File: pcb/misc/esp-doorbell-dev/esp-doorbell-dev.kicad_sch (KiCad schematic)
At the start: 26 parts, among them J1 JST XH, J2 Screw_Terminal_01x02, J3 JST XH/PH, J4 JST PH, Q1 BSS84, Q2 BSS84, Q3 BSS84, Q4 2N7002DW, Q5 BSS138, U1 WS2811F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

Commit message: Migrate `WS2811F` symbol from `lcsc` to `ic`
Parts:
- U1: symbol lcsc:WS2811F -> ic:WS2811F
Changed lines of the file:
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@@
 	)
 	(symbol
-		(lib_id "lcsc:WS2811F")
+		(lib_id "ic:WS2811F")
 		(at 105.41 44.45 0)
 		(unit 1)

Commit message: Migrate `LD2410C` symbol from `lcsc` to `modules`
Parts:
- SM4: symbol lcsc:HLK-LD2410C-P -> modules:LD2410C
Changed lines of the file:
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@@
 	)
 	(symbol
-		(lib_id "lcsc:HLK-LD2410C-P")
+		(lib_id "modules:LD2410C")
 		(at 255.27 41.91 0)
 		(unit 1)

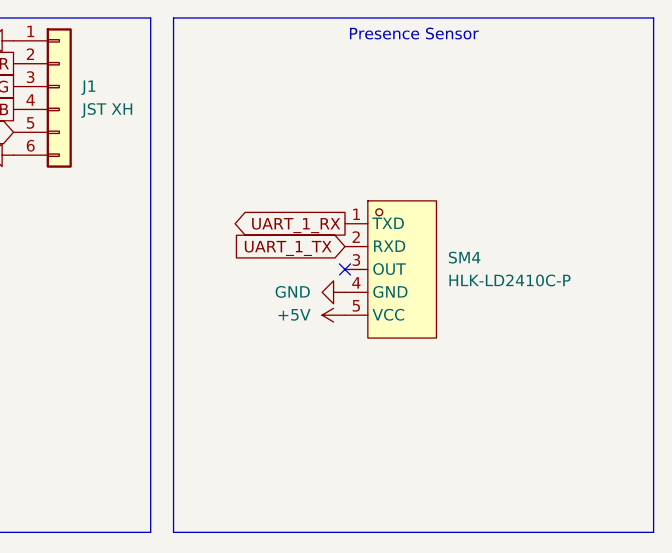
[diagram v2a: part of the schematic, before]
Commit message: Rework `HLK-LD2410C` to match KiCAD symbol conventions
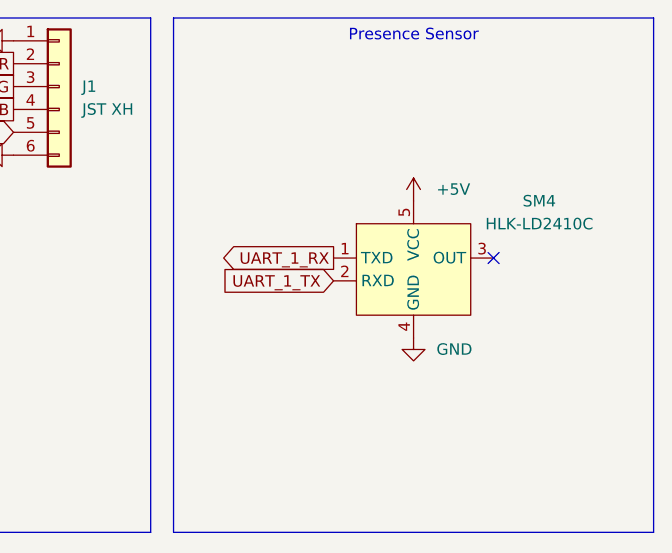
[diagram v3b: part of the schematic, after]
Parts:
- removed SM4: HLK-LD2410C-P, lcsc:SENSOR-TH_HLK-LD2410C-P, symbol modules:LD2410C
- added SM4: HLK-LD2410C, lcsc:SENSOR-TH_HLK-LD2410C-P, symbol module:HLK-LD2410C
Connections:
- net +5V: now also SM4.5 (VCC)
- net GND: now also SM4.4 (GND)
- net UART_1_RX: now also SM4.1 (TXD)
- net UART_1_TX: now also SM4.2 (RXD)
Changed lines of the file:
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@@
 	)
 	(no_connect
-		(at 248.92 41.91)
+		(at 265.43 40.64)
 	)
 	(no_connect
@@
 	(global_label "UART_1_TX"
 		(shape input)
-		(at 248.92 39.37 180)
+		(at 247.65 43.18 180)
 		(fields_autoplaced yes)
 		(effects
@@
 		)
 		(property "Intersheetrefs" "${INTERSHEET_REFS}"
-			(at 235.9563 39.37 0)
+			(at 234.6863 43.18 0)
 			(effects
 				(font
@@
 	(global_label "UART_1_RX"
 		(shape output)
-		(at 248.92 36.83 180)
+		(at 247.65 40.64 180)
 		(fields_autoplaced yes)
 		(effects
@@
 		)
 		(property "Intersheetrefs" "${INTERSHEET_REFS}"
-			(at 235.6539 36.83 0)
+			(at 234.3839 40.64 0)
 			(effects
 				(font
@@
 	(symbol
 		(lib_id "power:GND")
-		(at 248.92 44.45 270)
+		(at 256.54 49.53 0)
 		(unit 1)
 		(exclude_from_sim no)
@@
 		(fields_autoplaced yes)
 		(property "Reference" "#PWR010"
-			(at 242.57 44.45 0)
+			(at 256.54 55.88 0)
 			(effects
 				(font
@@
 		)
 		(property "Value" "GND"
-			(at 245.11 44.4499 90)
+			(at 259.08 50.7999 0)
 			(effects
 				(font
 					(size 1.27 1.27)
 				)
-				(justify right)
+				(justify left)
 			)
 		)
 		(property "Footprint" ""
-			(at 248.92 44.45 0)
+			(at 256.54 49.53 0)
 			(effects
 				(font
@@
 		)
 		(property "Datasheet" ""
-			(at 248.92 44.45 0)
+			(at 256.54 49.53 0)
 			(effects
 				(font
@@
 		)
 		(property "Description" "Power symbol creates a global label with name \"GND\" , ground"
-			(at 248.92 44.45 0)
+			(at 256.54 49.53 0)
 			(effects
 				(font
@@
 	)
 	(symbol
-		(lib_id "modules:LD2410C")
-		(at 255.27 41.91 0)
-		(unit 1)
-		(exclude_from_sim no)
-		(in_bom yes)
-		(on_board yes)
-		(dnp no)
-		(fields_autoplaced yes)
-		(property "Reference" "SM4"
-			(at 260.35 40.6399 0)
-			(effects
-				(font
-					(size 1.27 1.27)
-				)
-				(justify left)
-			)
-		)
-		(property "Value" "HLK-LD2410C-P"
-			(at 260.35 43.1799 0)
-			(effects
-				(font
-					(size 1.27 1.27)
-				)
-				(justify left)
-			)
-		)
-		(property "Footprint" "lcsc:SENSOR-TH_HLK-LD2410C-P"
-			(at 255.27 54.61 0)
-			(effects
-				(font
-					(size 1.27 1.27)
-				)
-				(hide yes)
-			)
-		)
-		(property "Datasheet" ""
-			(at 255.27 41.91 0)
-			(effects
-				(font
-					(size 1.27 1.27)
-				)
-				(hide yes)
-			)
-		)
-		(property "Description" ""
-			(at 255.27 41.91 0)
-			(effects
-				(font
-					(size 1.27 1.27)
-				)
-				(hide yes)
-			)
-		)
-		(property "LCSC Part" "C19723500"
-			(at 255.27 57.15 0)
-			(effects
-				(font
-					(size 1.27 1.27)
-				)
-				(hide yes)
-			)
-		)
-		(pin "1"
-		)
-		(pin "3"
-		)
-		(pin "2"
-		)
-		(pin "4"
-		)
-		(pin "5"
-		)
-		(instances
-			(project ""
-				(path "/76a56607-25e2-40a3-9282-ff279b153f75"
-					(reference "SM4")
-					(unit 1)
-				)
-			)
-		)
-	)
-	(symbol
 		(lib_id "power:+5V")
 		(at 137.16 86.36 90)
@@
 	(symbol
 		(lib_id "power:+5V")
-		(at 248.92 46.99 90)
+		(at 256.54 34.29 0)
 		(unit 1)
 		(exclude_from_sim no)
@@
 		(fields_autoplaced yes)
 		(property "Reference" "#PWR09"
-			(at 252.73 46.99 0)
+			(at 256.54 38.1 0)
 			(effects
 				(font
@@
 		)
 		(property "Value" "+5V"
-			(at 245.11 46.9899 90)
+			(at 259.08 33.0199 0)
 			(effects
 				(font
@@
 		)
 		(property "Footprint" ""
-			(at 248.92 46.99 0)
+			(at 256.54 34.29 0)
 			(effects
 				(font
@@
 		)
 		(property "Datasheet" ""
-			(at 248.92 46.99 0)
+			(at 256.54 34.29 0)
 			(effects
 				(font
@@
 		)
 		(property "Description" "Power symbol creates a global label with name \"+5V\""
-			(at 248.92 46.99 0)
+			(at 256.54 34.29 0)
 			(effects
 				(font
@@
 					(unit 1)
 				)
+			)
+		)
+	)
+	(symbol
+		(lib_id "module:HLK-LD2410C")
+		(at 256.54 41.91 0)
+		(unit 1)
+		(exclude_from_sim no)
+		(in_bom yes)
+		(on_board yes)
+		(dnp no)
+		(fields_autoplaced yes)
+		(property "Reference" "SM4"
+			(at 270.51 34.3214 0)
+			(effects
+				(font
+					(size 1.27 1.27)
+				)
+			)
+		)
+		(property "Value" "HLK-LD2410C"
+			(at 270.51 36.8614 0)
+			(effects
+				(font
+					(size 1.27 1.27)
+				)
+			)
+		)
+		(property "Footprint" "lcsc:SENSOR-TH_HLK-LD2410C-P"
+			(at 256.54 54.61 0)
+			(effects
+				(font
+					(size 1.27 1.27)
+				)
+				(hide yes)
+			)
+		)
+		(property "Datasheet" "https://www.lcsc.com/datasheet/lcsc_datasheet_2409141622_HI-LINK-HLK-LD2410C-P_C19723500.pdf"
+			(at 275.59 46.99 0)
+			(effects
+				(font
+					(size 1.27 1.27)
+				)
+				(hide yes)
+			)
+		)
+		(property "Description" "Human Presence Sensor, Millimeter Wave Radar, Bluetooth Low Energy/UART module"
+			(at 275.59 46.99 0)
+			(effects
+				(font
+					(size 1.27 1.27)
+				)
+				(hide yes)
+			)
+		)
+		(property "LCSC Part" "C19723500"
+			(at 256.54 57.15 0)
+			(effects
+				(font
+					(size 1.27 1.27)
+				)
+				(hide yes)
+			)
+		)
+		(pin "3"
+		)
+		(pin "5"
+		)
+		(pin "4"
+		)
+		(pin "2"
+		)
+		(pin "1"
+		)
+		(instances
+			(project ""
+				(path "/76a56607-25e2-40a3-9282-ff279b153f75"
+					(reference "SM4")
+					(unit 1)
+				)

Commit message: Migrate HLK-LD2410C module footprint from `lcsc` to `module`
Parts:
- SM4: footprint lcsc:SENSOR-TH_HLK-LD2410C-P -> module:HLK-LD2410C-module
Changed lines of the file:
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@@
 			)
 		)
-		(property "Footprint" "lcsc:SENSOR-TH_HLK-LD2410C-P"
+		(property "Footprint" "module:HLK-LD2410C-module"
 			(at 256.54 54.61 0)
 			(effects

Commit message: Migrate G3MB-202P footprint from `custom` to `discrete`
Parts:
- U2: footprint custom:RELAY-G3MB-202P-5VDC -> discrete:Relay_G3MB-202P
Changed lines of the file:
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@@
 			)
 		)
-		(property "Footprint" "custom:RELAY-G3MB-202P-5VDC"
+		(property "Footprint" "discrete:Relay_G3MB-202P"
 			(at 167.64 123.19 0)
 			(effects

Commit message: Migrate 3.5mm 1x02 terminal block footprint to `connector`
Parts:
- J2: footprint custom:TerminalBlock_Phoenix_PT-1,5-2-3.5-H_1x02_P3.50mm_Horizontal_custom -> connector:TerminalBlock_Phoenix_PT-1,5-2-3.5-H_1x02_P3.50mm_Horizontal
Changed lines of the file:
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@@
 			)
 		)
-		(property "Footprint" "custom:TerminalBlock_Phoenix_PT-1,5-2-3.5-H_1x02_P3.50mm_Horizontal_custom"
+		(property "Footprint" "connector:TerminalBlock_Phoenix_PT-1,5-2-3.5-H_1x02_P3.50mm_Horizontal"
 			(at 175.26 86.36 0)
 			(effects

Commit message: Reduce custom footprint use on esp-doorbell-dev
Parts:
- Q4: footprint package:SOT-363_SC-70-6 -> package:SOT-363_SC-70-6_HandSolder
- Q5: footprint package:SOT-23 -> Package_TO_SOT_SMD:SOT-23
- R3, R4, R5: footprint custom:R_0603_1608Metric_Pad0.98x0.95mm_HandSolder_simple -> Resistor_SMD:R_0603_1608Metric_Pad0.98x0.95mm_HandSolder
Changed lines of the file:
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@@
 	)
 	(symbol
-		(lib_id "Device:R_Small")
-		(at 125.73 83.82 90)
-		(mirror x)
-		(unit 1)
-		(exclude_from_sim no)
-		(in_bom yes)
-		(on_board yes)
-		(dnp no)
-		(property "Reference" "R3"
-			(at 125.73 88.9 90)
-			(effects
-				(font
-					(size 1.27 1.27)
-				)
-			)
-		)
-		(property "Value" "100R"
-			(at 125.73 86.36 90)
-			(effects
-				(font
-					(size 1.27 1.27)
-				)
-			)
-		)
-		(property "Footprint" "custom:R_0603_1608Metric_Pad0.98x0.95mm_HandSolder_simple"
-			(at 125.73 83.82 0)
-			(effects
-				(font
-					(size 1.27 1.27)
-				)
-				(hide yes)
-			)
-		)
-		(property "Datasheet" "~"
-			(at 125.73 83.82 0)
-			(effects
-				(font
-					(size 1.27 1.27)
-				)
-				(hide yes)
-			)
-		)
-		(property "Description" "Resistor, small symbol"
-			(at 125.73 83.82 0)
-			(effects
-				(font
-					(size 1.27 1.27)
-				)
-				(hide yes)
-			)
-		)
-		(pin "2"
-		)
-		(pin "1"
-		)
-		(instances
-			(project "esp-door"
-				(path "/76a56607-25e2-40a3-9282-ff279b153f75"
-					(reference "R3")
-					(unit 1)
-				)
-			)
-		)
-	)
-	(symbol
 		(lib_id "power:GND")
 		(at 119.38 182.88 90)
@@
 			)
 		)
-		(property "Footprint" "package:SOT-23"
+		(property "Footprint" "Package_TO_SOT_SMD:SOT-23"
 			(at 153.035 123.19 0)
 			(effects
@@
 	)
 	(symbol
+		(lib_id "Device:R_Small")
+		(at 125.73 83.82 90)
+		(unit 1)
+		(exclude_from_sim no)
+		(in_bom yes)
+		(on_board yes)
+		(dnp no)
+		(fields_autoplaced yes)
+		(property "Reference" "R3"
+			(at 125.73 78.74 90)
+			(effects
+				(font
+					(size 1.27 1.27)
+				)
+			)
+		)
+		(property "Value" "100R"
+			(at 125.73 81.28 90)
+			(effects
+				(font
+					(size 1.27 1.27)
+				)
+			)
+		)
+		(property "Footprint" "Resistor_SMD:R_0603_1608Metric_Pad0.98x0.95mm_HandSolder"
+			(at 125.73 83.82 0)
+			(effects
+				(font
+					(size 1.27 1.27)
+				)
+				(hide yes)
+			)
+		)
+		(property "Datasheet" "~"
+			(at 125.73 83.82 0)
+			(effects
+				(font
+					(size 1.27 1.27)
+				)
+				(hide yes)
+			)
+		)
+		(property "Description" "Resistor, small symbol"
+			(at 125.73 83.82 0)
+			(effects
+				(font
+					(size 1.27 1.27)
+				)
+				(hide yes)
+			)
+		)
+		(pin "2"
+		)
+		(pin "1"
+		)
+		(instances
+			(project ""
+				(path "/76a56607-25e2-40a3-9282-ff279b153f75"
+					(reference "R3")
+					(unit 1)
+				)
+			)
+		)
+	)
+	(symbol
 		(lib_id "power:GND")
 		(at 119.38 180.34 90)
@@
 			)
 		)
-		(property "Footprint" "package:SOT-363_SC-70-6"
+		(property "Footprint" "package:SOT-363_SC-70-6_HandSolder"
 			(at 186.055 154.94 0)
 			(effects
@@
 			)
 		)
-		(property "Footprint" "custom:R_0603_1608Metric_Pad0.98x0.95mm_HandSolder_simple"
+		(property "Footprint" "Resistor_SMD:R_0603_1608Metric_Pad0.98x0.95mm_HandSolder"
 			(at 147.32 110.49 0)
 			(effects
@@
 			)
 		)
-		(property "Footprint" "custom:R_0603_1608Metric_Pad0.98x0.95mm_HandSolder_simple"
+		(property "Footprint" "Resistor_SMD:R_0603_1608Metric_Pad0.98x0.95mm_HandSolder"
 			(at 125.73 160.02 0)
 			(effects
@@
 			)
 		)
-		(property "Footprint" "package:SOT-363_SC-70-6"
+		(property "Footprint" "package:SOT-363_SC-70-6_HandSolder"
 			(at 252.095 154.94 0)
 			(effects

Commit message: Migrate custom horizontal THT JST connector footprints to `connector`
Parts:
- J1: footprint custom:JST_XH_S6B-XH_1x06_P2.50mm_Horizontal -> connector:JST_XH_S6B-XH-2AW_1x06_P2.50mm_Horizontal
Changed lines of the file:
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@@
 			)
 		)
-		(property "Footprint" "custom:JST_XH_S6B-XH_1x06_P2.50mm_Horizontal"
+		(property "Footprint" "connector:JST_XH_S6B-XH-2AW_1x06_P2.50mm_Horizontal"
 			(at 217.17 21.59 0)
 			(effects
